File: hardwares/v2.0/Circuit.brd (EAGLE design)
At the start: 50 x 50 mm, 34 parts, among them IC1 TINY24/44/84-PU, IC2 HT-7733A, J1 1X2-3.5MM, Q1 8MHz, T1 2N2222, T2 2N2222, T3 2N2222, T4 2N2222, T5 2N2222, T6 2N2222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

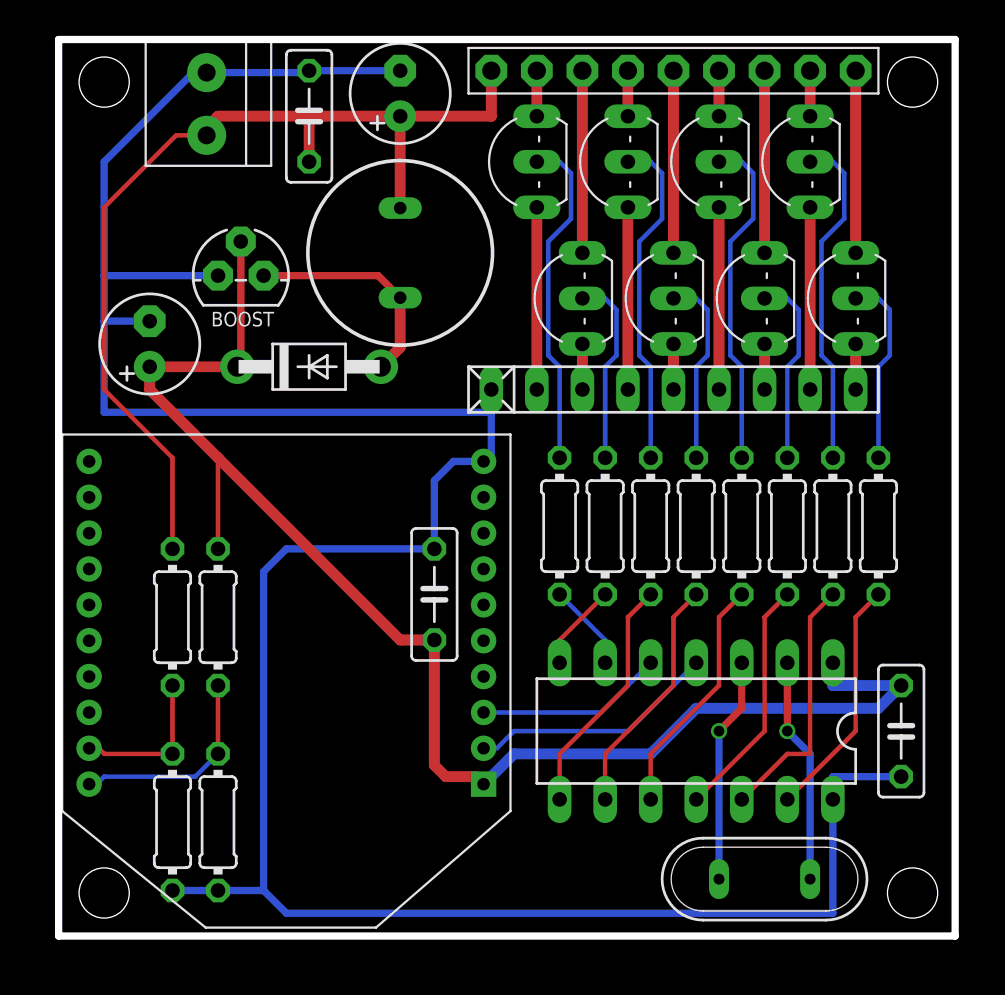
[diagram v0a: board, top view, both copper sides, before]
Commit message: Circuit: Add RESET sw
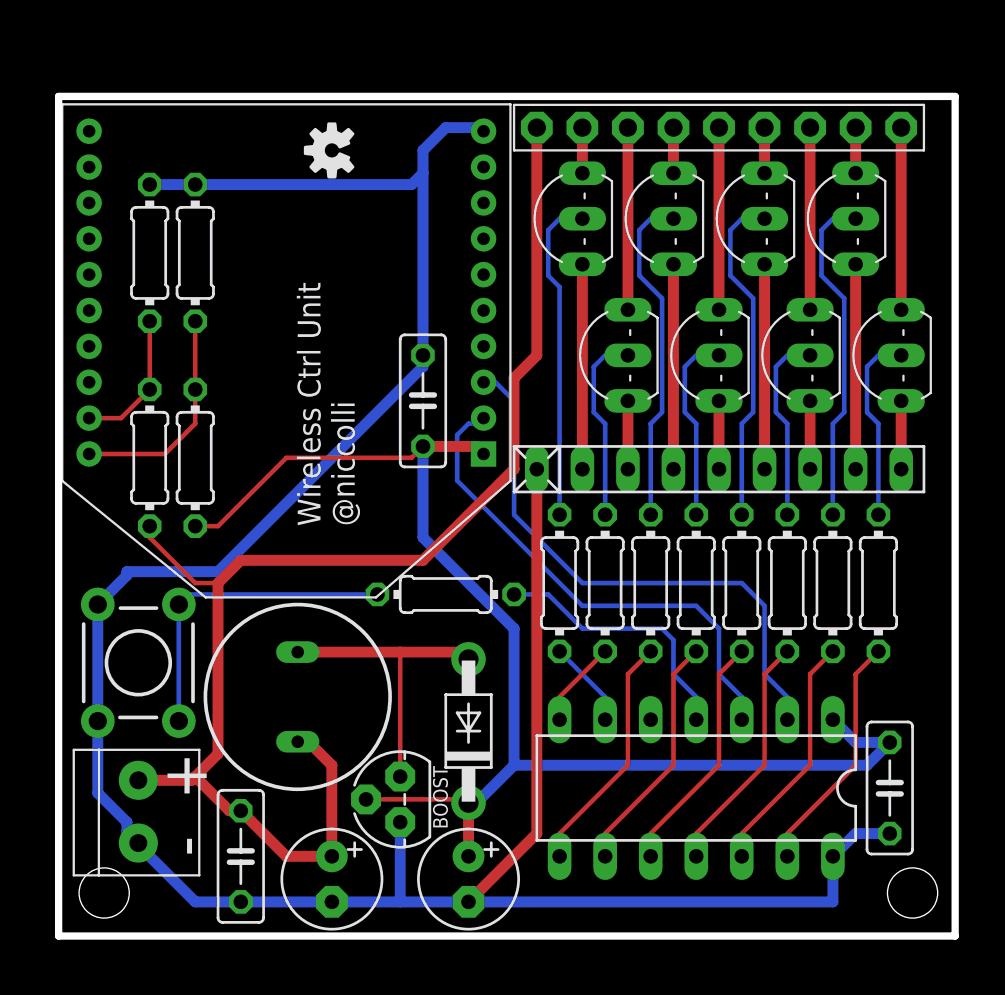
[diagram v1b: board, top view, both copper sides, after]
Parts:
- removed Q1: 8MHz, special:QS
- added R6: 1k, rcl:0204/7
- added S1: (no value), SparkFun:TACTILE-PTH
- added U$1: (no value), SparkFun:OSHW-LOGO-S
- moved C2 44.0 mm to (15.2, 3.17), turned to 270 degrees
- moved C1 41.5 mm to (10.2, 4.45), turned to 270 degrees
- moved J1 39.6 mm to (4.45, 6.99), turned to 270 degrees
- moved C3 34.7 mm to (22.9, 3.17), turned to 270 degrees
- moved R2 31.8 mm to (7.62, 38.1), turned to 270 degrees
- moved R4 31.8 mm to (5.08, 38.1), turned to 270 degrees
- moved IC2 30.5 mm to (19.1, 7.62), turned to 90 degrees
- moved L1 25.4 mm to (13.3, 13.3), turned to 90 degrees
- moved D1 22.2 mm to (22.9, 11.4), turned to 90 degrees
- moved U1 18.4 mm to (12.7, 32.4)
- moved C5 10.8 mm to (20.3, 29.8)
- moved R1 8.98 mm to (7.62, 26.7), turned to 270 degrees
- moved R3 8.98 mm to (5.08, 26.7), turned to 270 degrees
- moved RN1 5.12 mm to (36.8, 26.0)
- moved T2 4.07 mm to (30.5, 32.4)
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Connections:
- net GND: now also S1.1, S1.2
- net N$1: now also IC1.3; no longer IC1.4
- net N$2: now also IC1.2; no longer IC1.5
- net N$4: now also R6.1, S1.3, S1.4; no longer IC1.3, Q1.2
- net N$5: now also IC1.4, R6.2; no longer IC1.2, Q1.1
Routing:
- net V+: track 54.8 -> 75.8 mm
- net N$2: track 10.5 -> 31.4 mm
- net N$1: track 13.8 -> 28.0 mm
- net +3V3: track 80.8 -> 75.3 mm
- net N$4: track 12.6 -> 17.8 mm, vias 1 -> 0
- net GND: track 150.9 -> 146.1 mm
- net N$3: track 12.4 -> 16.6 mm
- net N$5: track 12.6 -> 14.9 mm, vias 1 -> 0
- net N$38: track 10.2 -> 11.4 mm
- net N$35: track 10.2 -> 11.4 mm
- net N$33: track 10.2 -> 11.4 mm
- net N$16: track 10.2 -> 11.4 mm
- net N$37: track 2.54 -> 3.81 mm
- net N$36: track 2.54 -> 3.81 mm
- net N$34: track 2.54 -> 3.81 mm
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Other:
- board size 50 x 50 mm -> 50 x 46.8 mm
- board text added: "+"
- board text added: "-"
- board text added: "LEDtie v2.0"
- board text added: "Wireless Ctrl Unit @niccolli"

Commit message: Circuit: GND pattern changed
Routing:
- net GND: track 146.1 -> 156.2 mm, vias 0 -> 25
- added copper zone on layer 1, net GND
- added copper zone on layer 16, net GND
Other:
- board text added: "Wireless Ctrl Unit github.com/niccolli"
- board text removed: "Wireless Ctrl Unit @niccolli"
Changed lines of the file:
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@@
 <hole x="47.625" y="2.4" drill="2.8"/>
 <hole x="2.54" y="2.4" drill="2.8"/>
-<text x="12.7" y="22.86" size="2.54" layer="27" font="vector" rot="R90">LEDtie v2.0</text>
+<text x="12.7" y="22.86" size="2.54" layer="25" font="vector" rot="R90">LEDtie v2.0</text>
 <text x="16.51" y="22.86" size="1.27" layer="25" font="vector" rot="R90">Wireless Ctrl Unit
-@niccolli</text>
+github.com/niccolli</text>
 <text x="8.255" y="7.62" size="2.54" layer="25" font="vector" rot="R90">+</text>
 <text x="8.255" y="4.445" size="2.54" layer="25" font="vector" rot="R90">-</text>
@@
 <contactref element="RN1" pad="1"/>
 <contactref element="J1" pad="1"/>
-<wire x1="4.445" y1="5.185" x2="4.445" y2="5.08" width="0.6096" layer="16"/>
-<wire x1="4.445" y1="5.08" x2="7.62" y2="1.905" width="0.6096" layer="16"/>
-<wire x1="7.62" y1="1.905" x2="10.16" y2="1.905" width="0.6096" layer="16"/>
-<wire x1="10.16" y1="1.905" x2="15.24" y2="1.905" width="0.6096" layer="16"/>
-<wire x1="22.86" y1="1.905" x2="19.05" y2="1.905" width="0.6096" layer="16"/>
-<wire x1="19.05" y1="1.905" x2="15.24" y2="1.905" width="0.6096" layer="16"/>
-<wire x1="22.86" y1="1.905" x2="43.18" y2="1.905" width="0.6096" layer="16"/>
-<wire x1="19.05" y1="6.35" x2="19.05" y2="1.905" width="0.6096" layer="16"/>
-<wire x1="20.32" y1="32.385" x2="20.32" y2="42.545" width="0.6096" layer="16"/>
+<wire x1="7.62" y1="1.905" x2="10.16" y2="1.905" width="0.254" layer="16"/>
+<wire x1="10.16" y1="1.905" x2="15.24" y2="1.905" width="0.254" layer="16"/>
+<wire x1="22.86" y1="1.905" x2="19.05" y2="1.905" width="0.254" layer="16"/>
+<wire x1="19.05" y1="1.905" x2="15.24" y2="1.905" width="0.254" layer="16"/>
+<wire x1="22.86" y1="1.905" x2="43.18" y2="1.905" width="0.254" layer="16"/>
+<wire x1="19.05" y1="6.35" x2="19.05" y2="1.905" width="0.254" layer="16"/>
+<wire x1="20.32" y1="32.385" x2="20.32" y2="42.545" width="0.254" layer="16"/>
 <wire x1="20.32" y1="42.545" x2="20.32" y2="43.815" width="0.6096" layer="16"/>
-<wire x1="20.32" y1="43.815" x2="21.59" y2="45.085" width="0.6096" layer="16"/>
-<wire x1="21.59" y1="45.085" x2="23.5" y2="45.085" width="0.6096" layer="16"/>
-<wire x1="23.5" y1="45.085" x2="23.7" y2="44.885" width="0.6096" layer="16"/>
-<wire x1="5.08" y1="41.91" x2="7.62" y2="41.91" width="0.6096" layer="16"/>
-<wire x1="7.62" y1="41.91" x2="19.685" y2="41.91" width="0.6096" layer="16"/>
+<wire x1="5.08" y1="41.91" x2="7.62" y2="41.91" width="0.254" layer="16"/>
+<wire x1="7.62" y1="41.91" x2="19.685" y2="41.91" width="0.254" layer="16"/>
 <wire x1="19.685" y1="41.91" x2="20.32" y2="42.545" width="0.6096" layer="16"/>
-<wire x1="46.355" y1="5.715" x2="44.45" y2="5.715" width="0.6096" layer="16"/>
-<wire x1="44.45" y1="5.715" x2="43.18" y2="4.445" width="0.6096" layer="16"/>
-<wire x1="43.18" y1="4.445" x2="43.18" y2="1.905" width="0.6096" layer="16"/>
-<wire x1="26.67" y1="26.035" x2="26.67" y2="5.715" width="0.6096" layer="1"/>
-<wire x1="26.67" y1="5.715" x2="22.86" y2="1.905" width="0.6096" layer="1"/>
-<wire x1="20.32" y1="32.385" x2="20.32" y2="31.75" width="0.6096" layer="16"/>
+<wire x1="43.18" y1="4.445" x2="43.18" y2="1.905" width="0.254" layer="16"/>
+<wire x1="26.67" y1="26.035" x2="26.67" y2="7.62" width="0.254" layer="1"/>
+<wire x1="26.67" y1="7.62" x2="26.67" y2="5.715" width="0.254" layer="1"/>
+<wire x1="26.67" y1="5.715" x2="26.67" y2="1.905" width="0.254" layer="1"/>
+<wire x1="26.67" y1="1.905" x2="22.86" y2="1.905" width="0.254" layer="1"/>
 <contactref element="S1" pad="1"/>
 <contactref element="S1" pad="2"/>
-<wire x1="20.32" y1="31.75" x2="8.89" y2="20.32" width="0.6096" layer="16"/>
-<wire x1="8.89" y1="20.32" x2="3.81" y2="20.32" width="0.6096" layer="16"/>
-<wire x1="3.81" y1="20.32" x2="3.81" y2="20.1168" width="0.6096" layer="16"/>
-<wire x1="3.81" y1="20.1168" x2="2.1844" y2="18.4912" width="0.6096" layer="16"/>
-<wire x1="2.1844" y1="18.4912" x2="2.1844" y2="11.9888" width="0.6096" layer="16"/>
-<wire x1="2.1844" y1="11.9888" x2="2.1844" y2="7.9756" width="0.6096" layer="16"/>
-<wire x1="2.1844" y1="7.9756" x2="3.81" y2="6.35" width="0.6096" layer="16"/>
-<wire x1="3.81" y1="6.35" x2="3.81" y2="5.82" width="0.6096" layer="16"/>
-<wire x1="3.81" y1="5.82" x2="4.445" y2="5.185" width="0.6096" layer="16"/>
+<wire x1="2.1844" y1="18.4912" x2="2.1844" y2="11.9888" width="0.254" layer="16"/>
+<wire x1="20.32" y1="32.385" x2="20.32" y2="30.48" width="0.254" layer="16"/>
+<wire x1="20.32" y1="30.48" x2="17.78" y2="27.94" width="0.6096" layer="16"/>
+<wire x1="17.78" y1="27.94" x2="11.43" y2="21.59" width="0.6096" layer="16"/>
+<wire x1="11.43" y1="21.59" x2="2.54" y2="21.59" width="0.6096" layer="16"/>
+<wire x1="2.54" y1="21.59" x2="2.1844" y2="21.59" width="0.6096" layer="16"/>
+<wire x1="2.1844" y1="21.59" x2="2.1844" y2="18.4912" width="0.254" layer="16"/>
+<wire x1="2.1844" y1="11.9888" x2="2.1844" y2="5.4356" width="0.254" layer="16"/>
+<wire x1="2.1844" y1="5.4356" x2="2.54" y2="5.08" width="0.254" layer="16"/>
+<wire x1="2.54" y1="5.08" x2="4.34" y2="5.08" width="0.254" layer="16"/>
+<wire x1="4.34" y1="5.08" x2="4.445" y2="5.185" width="0.254" layer="16"/>
+<wire x1="4.445" y1="5.08" x2="4.445" y2="3.175" width="0.254" layer="16"/>
+<wire x1="4.445" y1="3.175" x2="5.08" y2="2.54" width="0.254" layer="16"/>
+<wire x1="5.08" y1="2.54" x2="6.985" y2="2.54" width="0.254" layer="16"/>
+<wire x1="6.985" y1="2.54" x2="7.62" y2="1.905" width="0.254" layer="16"/>
+<wire x1="23.7" y1="44.885" x2="22.025" y2="44.885" width="0.254" layer="16"/>
+<wire x1="22.025" y1="44.885" x2="21.59" y2="44.45" width="0.254" layer="16"/>
+<wire x1="21.59" y1="44.45" x2="20.955" y2="44.45" width="0.254" layer="16"/>
+<wire x1="20.955" y1="44.45" x2="20.32" y2="43.815" width="0.254" layer="16"/>
+<polygon width="0.254" layer="16">
+<vertex x="-1.27" y="48.26"/>
+<vertex x="50.8" y="48.26"/>
+<vertex x="50.8" y="-1.27"/>
+<vertex x="-1.27" y="-1.27"/>
+</polygon>
+<wire x1="43.18" y1="4.445" x2="43.18" y2="6.985" width="0.254" layer="16"/>
+<wire x1="43.18" y1="6.985" x2="46.355" y2="6.985" width="0.254" layer="16"/>
+<wire x1="46.355" y1="6.985" x2="46.355" y2="5.715" width="0.254" layer="16"/>
+<polygon width="0.254" layer="1">
+<vertex x="-1.27" y="-1.27"/>
+<vertex x="50.8" y="-1.27"/>
+<vertex x="50.8" y="48.26"/>
+<vertex x="-1.27" y="48.26"/>
+</polygon>
+<via x="17.78" y="27.94" extent="1-16" drill="0.5"/>
+<via x="2.54" y="21.59" extent="1-16" drill="0.5"/>
+<via x="26.67" y="7.62" extent="1-16" drill="0.5"/>
+<via x="27.94" y="1.27" extent="1-16" drill="0.5"/>
+<via x="33.02" y="1.27" extent="1-16" drill="0.5"/>
+<via x="38.1" y="1.27" extent="1-16" drill="0.5"/>
+<via x="43.18" y="1.27" extent="1-16" drill="0.5"/>
+<via x="48.26" y="7.62" extent="1-16" drill="0.5"/>
+<via x="48.26" y="13.97" extent="1-16" drill="0.5"/>
+<via x="20.32" y="11.43" extent="1-16" drill="0.5"/>
+<via x="12.7" y="7.62" extent="1-16" drill="0.5"/>
+<via x="6.35" y="1.27" extent="1-16" drill="0.5"/>
+<via x="1.27" y="7.62" extent="1-16" drill="0.5"/>
+<via x="17.78" y="17.145" extent="1-16" drill="0.5"/>
+<via x="21.59" y="17.145" extent="1-16" drill="0.5"/>
+<via x="23.495" y="21.59" extent="1-16" drill="0.5"/>
+<via x="17.78" y="22.86" extent="1-16" drill="0.5"/>
+<via x="17.78" y="33.02" extent="1-16" drill="0.5"/>
+<via x="17.78" y="38.1" extent="1-16" drill="0.5"/>
+<via x="17.78" y="44.45" extent="1-16" drill="0.5"/>
+<via x="5.08" y="44.45" extent="1-16" drill="0.5"/>
+<via x="48.26" y="20.32" extent="1-16" drill="0.5"/>
+<via x="48.26" y="38.1" extent="1-16" drill="0.5"/>
+<via x="48.26" y="43.18" extent="1-16" drill="0.5"/>
+<via x="26.67" y="29.21" extent="1-16" drill="0.5"/>
 </signal>
 <signal name="+3V3">

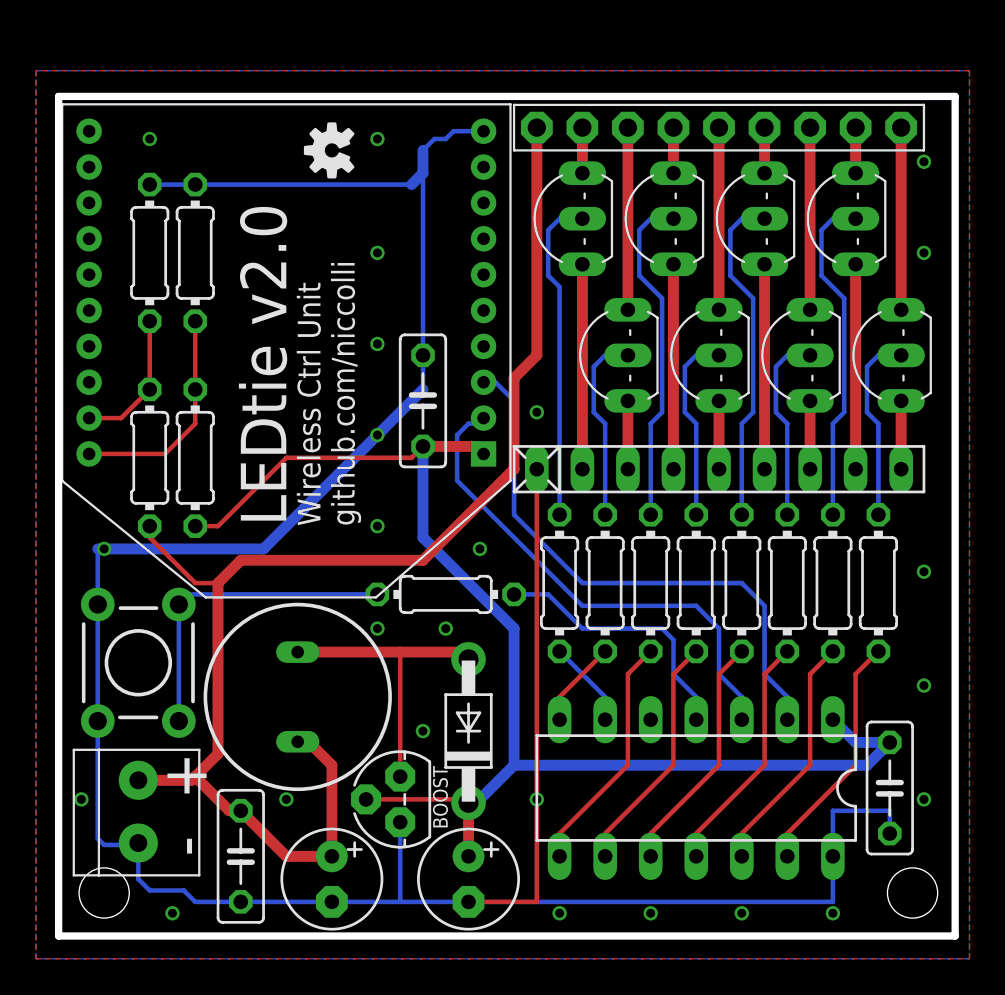
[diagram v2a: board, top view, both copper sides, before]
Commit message: Circuit: NPN Transistors changed
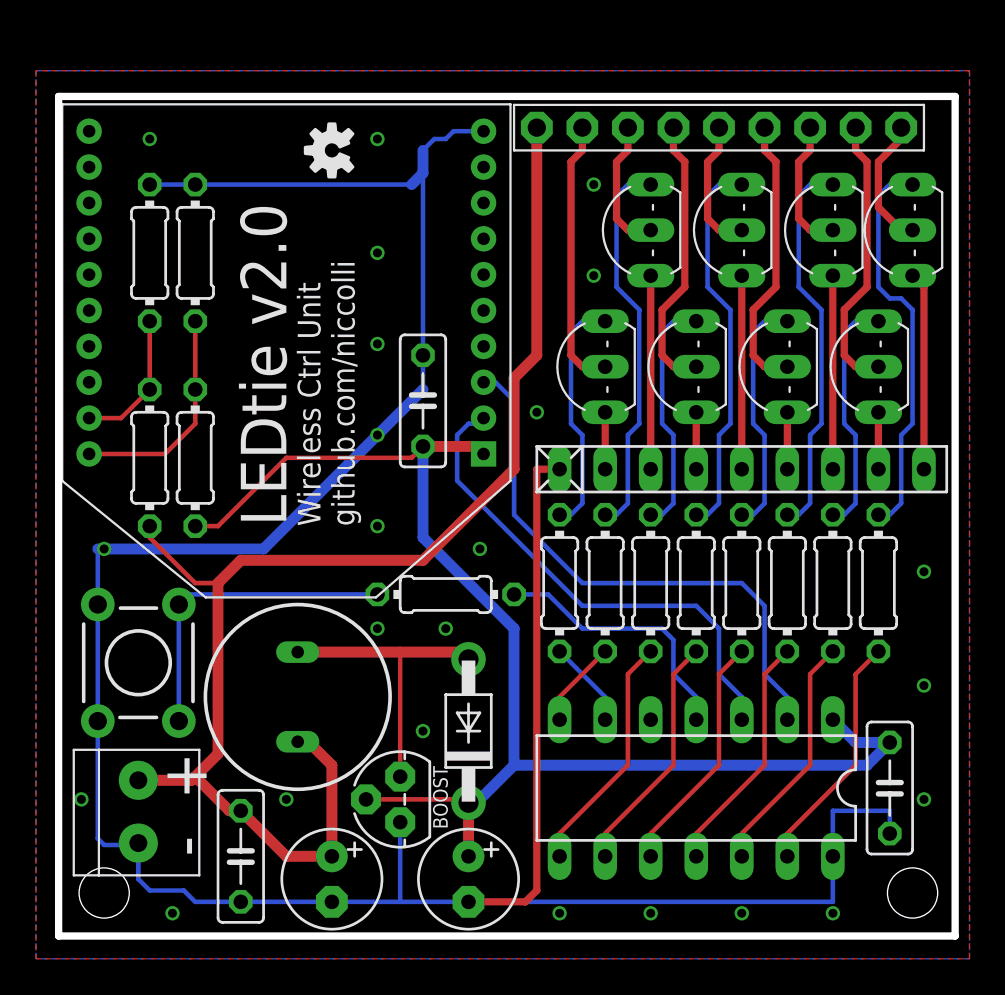
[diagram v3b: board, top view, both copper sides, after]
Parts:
- T1, T2, T3, T4, T5, T6, T7, T8: value 2N2222 -> 2SC1815; device adafruit:TO92-EBC-OVAL -> transistor:TO92-ECB
- moved T1 8.64 mm to (30.5, 31.8)
- moved T3 8.64 mm to (35.6, 31.8)
- moved T5 8.64 mm to (40.6, 31.8)
- moved T7 8.64 mm to (45.7, 31.8)
- moved T2 7.43 mm to (33.0, 39.4)
- moved T4 7.43 mm to (38.1, 39.4)
- moved T6 7.43 mm to (43.2, 39.4)
- moved T8 7.24 mm to (47.6, 39.4)
- moved RN1 1.27 mm to (38.1, 26.0)
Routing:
- net N$21: track 2.54 -> 15.7 mm
- net N$27: track 2.54 -> 15.7 mm
- net N$15: track 2.54 -> 15.7 mm
- net N$7: track 2.54 -> 15.1 mm
- net N$29: track 10.7 -> 22.3 mm
- net N$23: track 10.7 -> 21.6 mm
- net N$11: track 10.7 -> 21.6 mm
- net N$17: track 10.7 -> 21.6 mm
- net N$38: track 11.4 -> 3.18 mm
- net N$35: track 11.4 -> 3.18 mm
- net N$33: track 11.4 -> 3.18 mm
- net N$16: track 11.4 -> 3.18 mm
- net N$37: track 3.81 -> 11.1 mm
- net N$36: track 3.81 -> 10.8 mm
- net N$34: track 3.81 -> 10.8 mm
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
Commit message: Circuit fixed
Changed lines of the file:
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@@
 <via x="6.35" y="1.27" extent="1-16" drill="0.5"/>
 <via x="1.27" y="7.62" extent="1-16" drill="0.5"/>
-<via x="17.78" y="17.145" extent="1-16" drill="0.5"/>
-<via x="21.59" y="17.145" extent="1-16" drill="0.5"/>
+<via x="25.4" y="6.985" extent="1-16" drill="0.5"/>
+<via x="19.05" y="17.145" extent="1-16" drill="0.5"/>
 <via x="23.495" y="21.59" extent="1-16" drill="0.5"/>
 <via x="17.78" y="22.86" extent="1-16" drill="0.5"/>
@@
 <via x="29.845" y="41.91" extent="1-16" drill="0.5"/>
 <via x="29.845" y="36.83" extent="1-16" drill="0.5"/>
-<via x="26.67" y="29.21" extent="1-16" drill="0.5"/>
+<via x="27.305" y="29.21" extent="1-16" drill="0.5"/>
 <wire x1="27.94" y1="26.035" x2="26.67" y2="26.035" width="0.4064" layer="1"/>
 <wire x1="26.67" y1="26.035" x2="26.67" y2="2.54" width="0.4064" layer="1"/>
 <wire x1="26.67" y1="2.54" x2="26.035" y2="1.905" width="0.4064" layer="1"/>
 <wire x1="26.035" y1="1.905" x2="22.86" y2="1.905" width="0.4064" layer="1"/>
-<wire x1="29.845" y1="36.83" x2="29.845" y2="41.91" width="0" layer="19" extent="1-1"/>
-<wire x1="48.26" y1="20.32" x2="29.845" y2="36.83" width="0" layer="19" extent="1-1"/>
-<wire x1="48.26" y1="13.97" x2="48.26" y2="20.32" width="0" layer="19" extent="1-1"/>
-<wire x1="48.26" y1="7.62" x2="48.26" y2="13.97" width="0" layer="19" extent="1-1"/>
-<wire x1="46.355" y1="6.985" x2="48.26" y2="7.62" width="0" layer="19" extent="16-16"/>
-<wire x1="4.445" y1="5.185" x2="4.445" y2="5.08" width="0" layer="19" extent="16-16"/>
-<wire x1="43.18" y1="1.27" x2="43.18" y2="1.905" width="0" layer="19" extent="16-16"/>
-<wire x1="6.35" y1="1.27" x2="7.62" y2="1.905" width="0" layer="19" extent="16-16"/>
-<wire x1="27.94" y1="1.27" x2="26.67" y2="2.54" width="0" layer="19" extent="1-1"/>
-<wire x1="1.27" y1="7.62" x2="2.1844" y2="5.4356" width="0" layer="19" extent="16-16"/>
-<wire x1="5.08" y1="44.45" x2="5.08" y2="41.91" width="0" layer="19" extent="1-1"/>
-<wire x1="17.78" y1="44.45" x2="20.32" y2="43.815" width="0" layer="19" extent="16-16"/>
-<wire x1="17.78" y1="33.02" x2="20.32" y2="32.385" width="0" layer="19" extent="1-1"/>
-<wire x1="26.67" y1="29.21" x2="26.67" y2="26.035" width="0" layer="19" extent="1-1"/>
-<wire x1="17.78" y1="38.1" x2="19.685" y2="41.91" width="0" layer="19" extent="16-16"/>
-<wire x1="17.78" y1="22.86" x2="17.78" y2="27.94" width="0" layer="19" extent="16-16"/>
-<wire x1="38.1" y1="1.27" x2="43.18" y2="1.27" width="0" layer="19" extent="1-1"/>
-<wire x1="33.02" y1="1.27" x2="27.94" y2="1.27" width="0" layer="19" extent="1-1"/>
-<wire x1="20.32" y1="11.43" x2="19.05" y2="6.35" width="0" layer="19" extent="1-1"/>
-<wire x1="23.495" y1="21.59" x2="26.67" y2="26.035" width="0" layer="19" extent="1-1"/>
-<wire x1="21.59" y1="17.145" x2="23.495" y2="21.59" width="0" layer="19" extent="1-1"/>
-<wire x1="17.78" y1="17.145" x2="21.59" y2="17.145" width="0" layer="19" extent="1-1"/>
-<wire x1="12.7" y1="7.62" x2="15.24" y2="1.905" width="0" layer="19" extent="1-1"/>
 </signal>
 <signal name="+3V3">
